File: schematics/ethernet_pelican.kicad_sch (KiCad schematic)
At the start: 4 parts, among them J6 RJ45-HANRUN

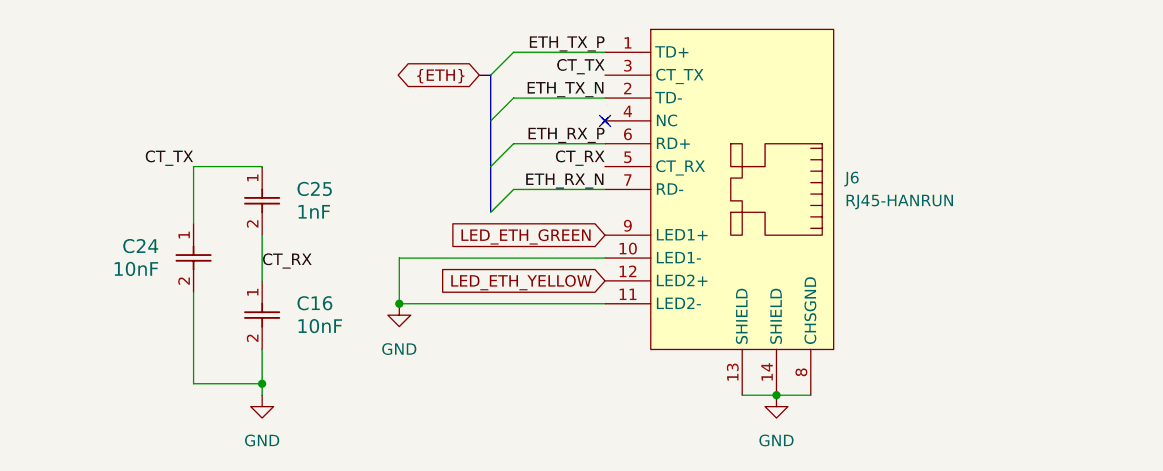
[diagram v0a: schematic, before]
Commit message: updated schematic based on review
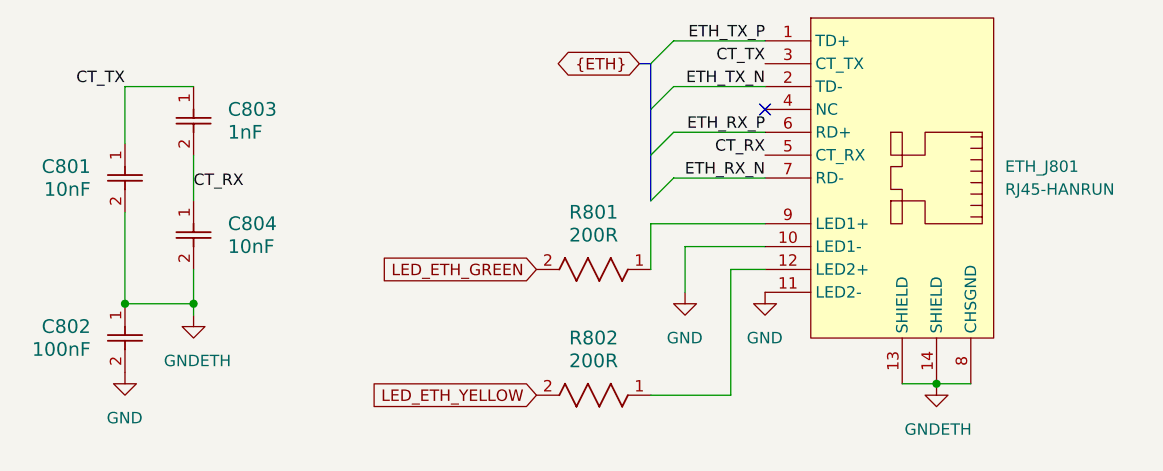
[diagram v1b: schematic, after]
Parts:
- added C802: 100nF, C_GRM155R71C104KA88D:C_GRM155R71C104KA88D, symbol C_GRM155R71C104KA88D:GRM155R71C104KA88D
- added R801, R802: 200R, R_RC0402FR:R_RC0402FR, symbol R_RC0402FR:RC0402FR-07200RL
- renumbered C24 to C801, C25 to C803, C16 to C804, J6 to ETH_J801
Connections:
- net GND: now also C802.2; no longer C801.2, C804.2, ETH_J801.13 (SHIELD), ETH_J801.14 (SHIELD), ETH_J801.8 (CHSGND)
- net LED_ETH_GREEN: now also R801.2; no longer ETH_J801.9 (LED1+)
- net LED_ETH_YELLOW: now also R802.2; no longer ETH_J801.12 (LED2+)
- new net: ETH_J801.12 (LED2+), R802.1
- new net: ETH_J801.9 (LED1+), R801.1
- new net GNDETH: C801.2, C802.1, C804.2, ETH_J801.13 (SHIELD), ETH_J801.14 (SHIELD), ETH_J801.8 (CHSGND)
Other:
- moved on the sheet: C801, C803, C804, ETH_J801
